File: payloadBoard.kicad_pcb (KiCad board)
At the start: 2 copper layers, 27 parts, among them J1 USB_C_Receptacle_USB2.0_16P, J2 SERVO, J3 2S Battery, U1 nRF52833_QDxx, U2 AT25SF041-SSHB-X, U3 LSM6DSO32

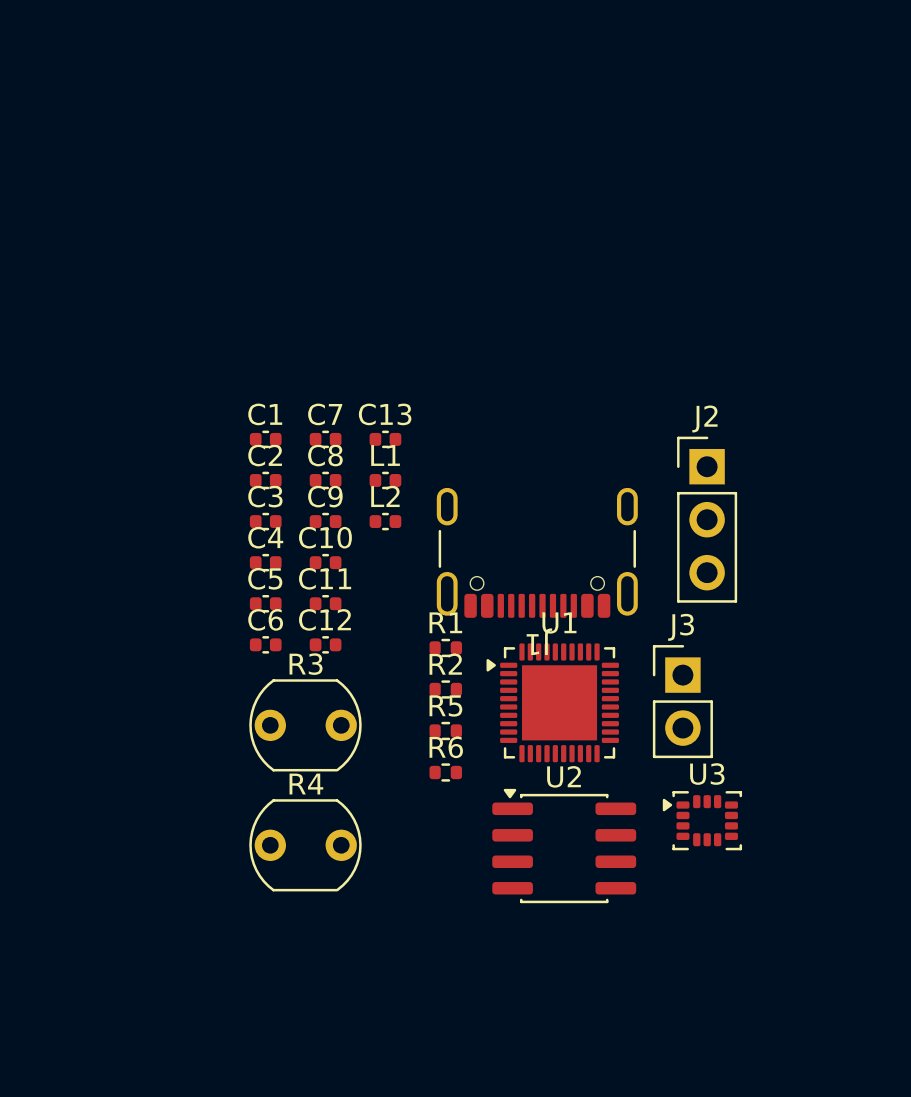
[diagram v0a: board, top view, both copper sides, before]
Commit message: all footprints in but antenna, review w. sophia done
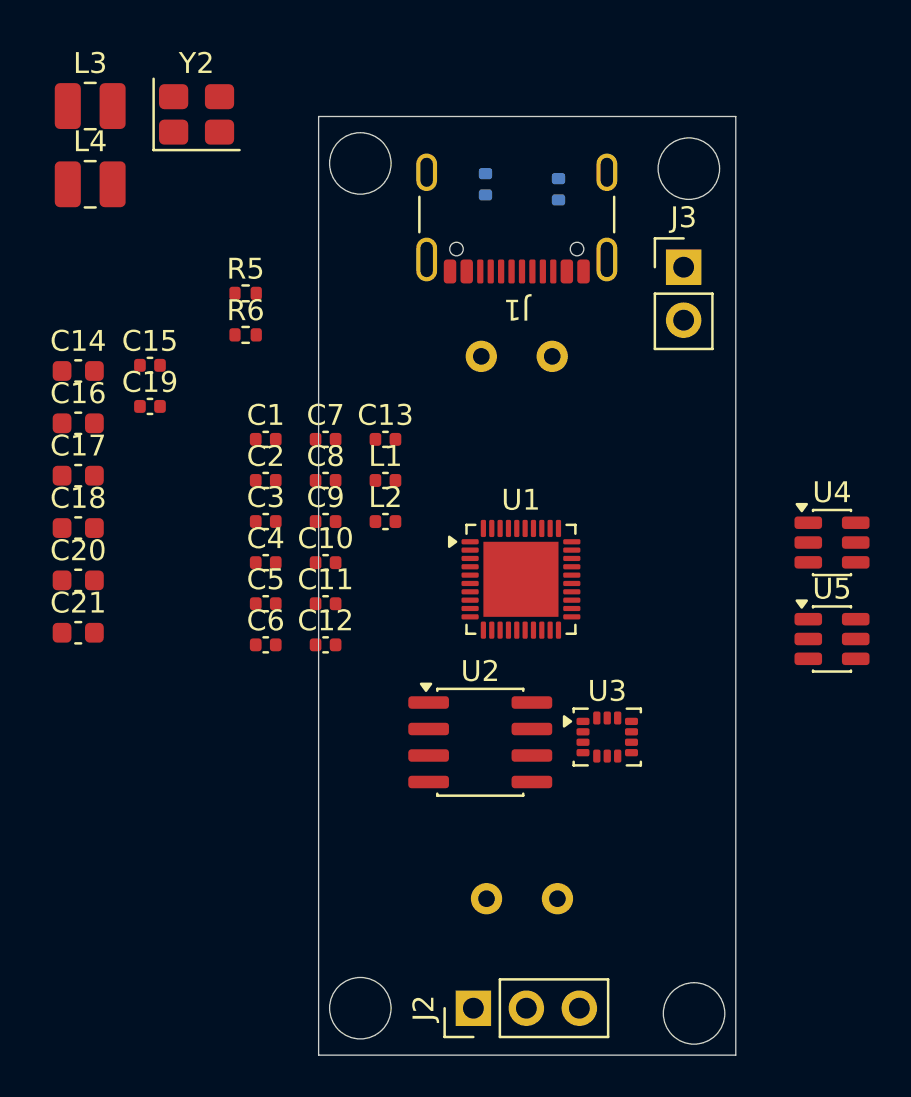
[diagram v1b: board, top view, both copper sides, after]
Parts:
- added C14: 10uF, Capacitor_SMD:C_0603_1608Metric, F.Cu at (135.0, 78.0)
- added C15: 100nF, Capacitor_SMD:C_0402_1005Metric, F.Cu at (138.4, 77.7)
- added C16: 22uF, Capacitor_SMD:C_0603_1608Metric, F.Cu at (135.0, 80.5)
- added C17: 22uF, Capacitor_SMD:C_0603_1608Metric, F.Cu at (135.0, 83.0)
- added C18: 10uF, Capacitor_SMD:C_0603_1608Metric, F.Cu at (135.0, 85.5)
- added C19: 100nF, Capacitor_SMD:C_0402_1005Metric, F.Cu at (138.4, 79.7)
- added C20: 22uF, Capacitor_SMD:C_0603_1608Metric, F.Cu at (135.0, 88.0)
- added C21: 22uF, Capacitor_SMD:C_0603_1608Metric, F.Cu at (135.0, 90.5)
- added L3: 4.7uH, Inductor_SMD:L_1008_2520Metric, F.Cu at (135.6, 65.2)
- added L4: 3.3uH, Inductor_SMD:L_1008_2520Metric, F.Cu at (135.6, 69.0)
- added U4: AP63205WU, Package_TO_SOT_SMD:TSOT-23-6, F.Cu at (171.1, 86.2)
- added U5: AP63203WU, Package_TO_SOT_SMD:TSOT-23-6, F.Cu at (171.1, 90.8)
- added Y2: Crystal_GND24, Crystal:Crystal_SMD_3225-4Pin_3.2x2.5mm, F.Cu at (140.7, 65.7)
- R1, R2, R3, R4: moved to B.Cu
- moved J2 28.3 mm to (153.9, 108.5), turned to 90 degrees
- moved R2 24.3 mm to (154.5, 69.0), turned to 90 degrees
- moved R6 23.1 mm to (143.0, 76.2)
- moved R5 23.1 mm to (143.0, 74.2)
- moved R1 22.6 mm to (158.0, 69.2), turned to 90 degrees
- moved R3 22.3 mm to (157.7, 77.2), turned to 180 degrees
- moved J3 19.6 mm to (164.0, 73.0)
- moved J1 16.1 mm to (156.0, 69.5)
- moved R4 14.0 mm to (157.9, 103.2), turned to 180 degrees
- moved U2 6.49 mm to (154.2, 95.8)
- moved U3 6.25 mm to (160.3, 95.5)
- moved U1 6.20 mm to (156.2, 87.9)
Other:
- board outline added: 20 x 45 mm
- board text added: "4x #4 Holes absolute max size 60x30mm"

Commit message: version 1 finished
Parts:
- added AE1: Antenna_Chip, RF_Antenna:Texas_SWRA117D_2.4GHz_Left, F.Cu at (150.6, 93.2)
- added C22: 1uF, Capacitor_SMD:C_0402_1005Metric, F.Cu at (161.5, 98.0)
- added J4: Conn_01x04, Connector_PinSocket_1.00mm:PinSocket_1x04_P1.00mm_Vertical, F.Cu at (146.6, 84.8)
- C14, C15, C16, C17, C18, C19, C20, C21, C7, L3, L4, U2, U4, U5: moved to B.Cu
- moved Y2 35.0 mm to (154.7, 97.7)
- moved R5 31.9 mm to (155.8, 103.4), turned to 90 degrees
- moved C18 29.8 mm to (163.9, 78.4), turned to -90 degrees
- moved C20 29.6 mm to (164.1, 82.9), turned to 90 degrees
- moved L4 29.0 mm to (160.3, 84.2), turned to -90 degrees
- moved C21 28.6 mm to (162.5, 82.9), turned to 90 degrees
- moved R4 26.5 mm to (154.3, 77.0), turned to 0 degrees
- moved U4 25.5 mm to (147.8, 75.9), turned to -90 degrees
- moved R3 25.0 mm to (154.3, 102.0), turned to 0 degrees
- moved C2 24.5 mm to (163.5, 98.0), turned to 90 degrees
- moved C19 21.8 mm to (160.1, 81.5)
- moved L3 20.1 mm to (147.6, 81.3), turned to -90 degrees
- moved C6 18.6 mm to (162.6, 89.7), turned to -90 degrees
- moved C11 18.0 mm to (162.5, 98.0), turned to -90 degrees
- moved C8 18.0 mm to (157.5, 97.7), turned to -90 degrees
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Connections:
- U1 pad 16: unconnected-(U1-P0.18/~{RESET}-Pad16) -> Net-(J4-Pin_1)
- U1 pad 17: unconnected-(U1-P0.20-Pad17) -> PWM
- U1 pad 19: unconnected-(U1-SWDIO-Pad19) -> Net-(J4-Pin_2)
- U1 pad 20: unconnected-(U1-SWDCLK-Pad20) -> Net-(J4-Pin_3)
- U1 pad 32: unconnected-(U1-AIN0/P0.02-Pad32) -> +5V_EN
- U1 pad 35: unconnected-(U1-AIN6/P0.30-Pad35) -> IMU_IRQ1
- U3 pad 4: IMU_IRQ -> IMU_IRQ1
- U4 pad 2: +BATT -> +5V_EN
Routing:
- net GND: track 0.00 -> 64.0 mm, vias 0 -> 49
- net +5V_EN: track 0.00 -> 35.1 mm, vias 0 -> 3
- net VBUS: track 0.00 -> 29.9 mm, vias 0 -> 1
- net ADC0: track 0.00 -> 28.2 mm, vias 0 -> 1
- net PWM: track 0.00 -> 26.4 mm, vias 0 -> 1
- net D-: track 0.00 -> 24.3 mm
- net D+: track 0.00 -> 24.2 mm
- net +3.3V: track 0.00 -> 22.9 mm, vias 0 -> 17
- net IMU_IRQ1: track 0.00 -> 18.2 mm, vias 0 -> 2
- net Net-(J4-Pin_1): track 0.00 -> 17.3 mm, vias 0 -> 1
- net Net-(J4-Pin_2): track 0.00 -> 14.9 mm
- net Net-(U1-DEC4): track 0.00 -> 13.9 mm, vias 0 -> 2
- net Net-(J4-Pin_3): track 0.00 -> 13.9 mm
- net CS: track 0.00 -> 12.5 mm, vias 0 -> 1
- net MISO: track 0.00 -> 10.8 mm, vias 0 -> 1
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- added copper zone on B.Cu, net +3.3V
- added copper zone on In2.Cu, net +3.3V
- added copper zone on B.Cu, net +5V
- added copper zone on In2.Cu, net +5V
- added copper zone on B.Cu, net +BATT
- added copper zone on B.Cu, net GND
- added copper zone on F.Cu, net GND
- added copper zone on In1.Cu, net GND
- added copper zone on B.Cu, net Net-(U4-SW)
- added copper zone on B.Cu, net Net-(U5-SW)
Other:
- outline, holes or cut-outs redrawn
- copper layers 2 -> 4
- board text added: "+BATT 3S MAX"
- board text added: "- 4x #4 Holes absolute max size 60x30mm"
- board text added: "GND"
- board text added: "Payload Deployment Board KV0R For Project Helios Nic DeBruin 2026"
- board text added: "SERVO"
- board text added: "USB-C"
- board text removed: "4x #4 Holes absolute max size 60x30mm"

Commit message: done other than funny silkscreen
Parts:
- added D1: LED, LED_SMD:LED_0603_1608Metric, F.Cu at (164.2, 84.7)
- added D2: LED, LED_SMD:LED_0603_1608Metric, F.Cu at (163.6, 101.7)
- added R7: 200, Resistor_SMD:R_0402_1005Metric, F.Cu at (164.2, 81.7)
- added R8: 200, Resistor_SMD:R_0402_1005Metric, F.Cu at (161.3, 102.5)
- added TP1: TestPoint, Antenna:0.75x0.75_TestPad, F.Cu at (158.2, 88.3)
- added TP2: TestPoint, Antenna:0.75x0.75_TestPad, F.Cu at (158.2, 87.0)
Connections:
- U1 pad 2: unconnected-(U1-XL1/P0.00-Pad2) -> LED
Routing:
- net LED: track 0.00 -> 6.94 mm
- net GND: track 64.0 -> 68.2 mm, vias 49 -> 50
- net Net-(D2-K): track 0.00 -> 1.80 mm
- net Net-(D1-K): track 0.00 -> 1.70 mm
- net +3.3V: track 22.9 -> 23.9 mm

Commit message: fixed impedance length to proper stackup
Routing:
- net GND: track 68.2 -> 59.1 mm
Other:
- board text added: "JLCJLCJLCJLC"
- board text removed: "- 4x #4 Holes absolute max size 60x30mm"
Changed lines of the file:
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@@
 			(outputformat 1)
 			(mirror no)
-			(drillshape 1)
+			(drillshape 0)
 			(scaleselection 1)
-			(outputdirectory "")
+			(outputdirectory "fab/")
 		)
 	)
@@
 		)
 	)
-	(gr_text "- 4x #4 Holes\n\nabsolute max size\n60x30mm"
-		(at 181.5 96.1 0)
-		(layer "Cmts.User")
+	(gr_text "JLCJLCJLCJLC"
+		(at 164.2 86.6 90)
+		(layer "B.SilkS")
 		(effects
 			(font
@@
 				(thickness 0.1)
 			)
-			(justify left bottom)
+			(justify left bottom mirror)
 		)
 	)
@@
 	)
 	(segment
-		(start 154.5 69)
-		(end 156.5 69)
-		(width 0.3)
-		(layer "B.Cu")
-		(net 1)
-	)
-	(segment
-		(start 159.765 69)
-		(end 162.5 71.735)
-		(width 0.3)
-		(layer "B.Cu")
-		(net 1)
-	)
-	(segment
-		(start 156.5 69)
-		(end 159.765 69)
-		(width 0.3)
-		(layer "B.Cu")
-		(net 1)
-	)
-	(segment
 		(start 164.2 85.4875)
 		(end 164.0125 85.4875)
@@
 		(start 155.605 93.175)
 		(end 156.625 93.175)
-		(width 0.1539)
+		(width 0.3244)
 		(layer "F.Cu")
 		(net 9)
@@
 		(start 156.7 93.25)
 		(end 157.9625 93.25)
-		(width 0.1539)
+		(width 0.3)
 		(layer "F.Cu")
 		(net 9)
@@
 		(start 156.625 93.175)
 		(end 156.65 93.2)
-		(width 0.1483)
+		(width 0.3244)
 		(layer "F.Cu")
 		(net 9)
@@
 		(start 156.65 93.2)
 		(end 156.7 93.25)
-		(width 0.1483)
+		(width 0.3244)
 		(layer "F.Cu")
 		(net 9)
@@
 		(start 154.62 93.2)
 		(end 154.645 93.175)
-		(width 0.1483)
+		(width 0.3244)
 		(layer "F.Cu")
 		(net 10)
@@
 		(start 152.61 93.2)
 		(end 153.63 93.2)
-		(width 0.1539)
+		(width 0.3244)
 		(layer "F.Cu")
 		(net 10)
@@
 		(start 153.63 93.2)
 		(end 154.62 93.2)
-		(width 0.1539)
+		(width 0.3244)
 		(layer "F.Cu")
 		(net 10)
@@
 		(start 151.65 93.2)
 		(end 150.6 93.2)
-		(width 0.1539)
+		(width 0.3244)
 		(layer "F.Cu")
 		(net 53)

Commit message: board done, plenty small
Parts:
- moved R7 0.65 mm to (164.2, 81.1)
- moved D1 0.53 mm to (164.1, 84.2)
- moved C20 0.53 mm to (164.2, 82.4)
- moved C21 0.53 mm to (162.6, 82.4)
- moved C19 0.53 mm to (160.2, 81.0)
- moved L4 0.53 mm to (160.3, 83.7)
- moved U5 0.53 mm to (161.3, 78.3)
- moved C18 0.53 mm to (163.9, 77.8)
- moved J4 0.22 mm to (146.7, 85.0)
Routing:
- net IMU_IRQ1: track 18.2 -> 20.6 mm
- net GND: track 59.1 -> 58.1 mm, vias 50 -> 45
- net +3.3V: track 23.9 -> 24.6 mm, vias 17 -> 13
- net CS: track 12.5 -> 13.1 mm
- net Net-(J4-Pin_1): vias 1 -> 0
